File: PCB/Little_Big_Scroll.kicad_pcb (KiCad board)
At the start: 2 copper layers, 83.6 x 40 mm, 22 parts, among them J1 Conn_01x02, SW1 SW_Push, SW2 SW_Push, SW3 SW_Push, SW4 SW_Push, SW7 Rotary_Encoder_Switch, U1 ProMicro

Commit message: folders
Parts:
- added Lic1: CC-BY-SA_4.0, Keyboard Library:CC_BY_SA_40, F.Cu at (234.2, 111.9)
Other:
- board text added: "JLCJLCJLCJLC"
- board text added: "Little Big Scroll v1.0 Markus Knutsson 2021 https://github.com/TweetyDaBird"
- board text removed: "Little Big Scroll v1.0 Markus Knutsson 2021 https://github.com/TweetyDaBird Licensed under CERN-OHL-S v2+ JLCJLCJLCJLC"

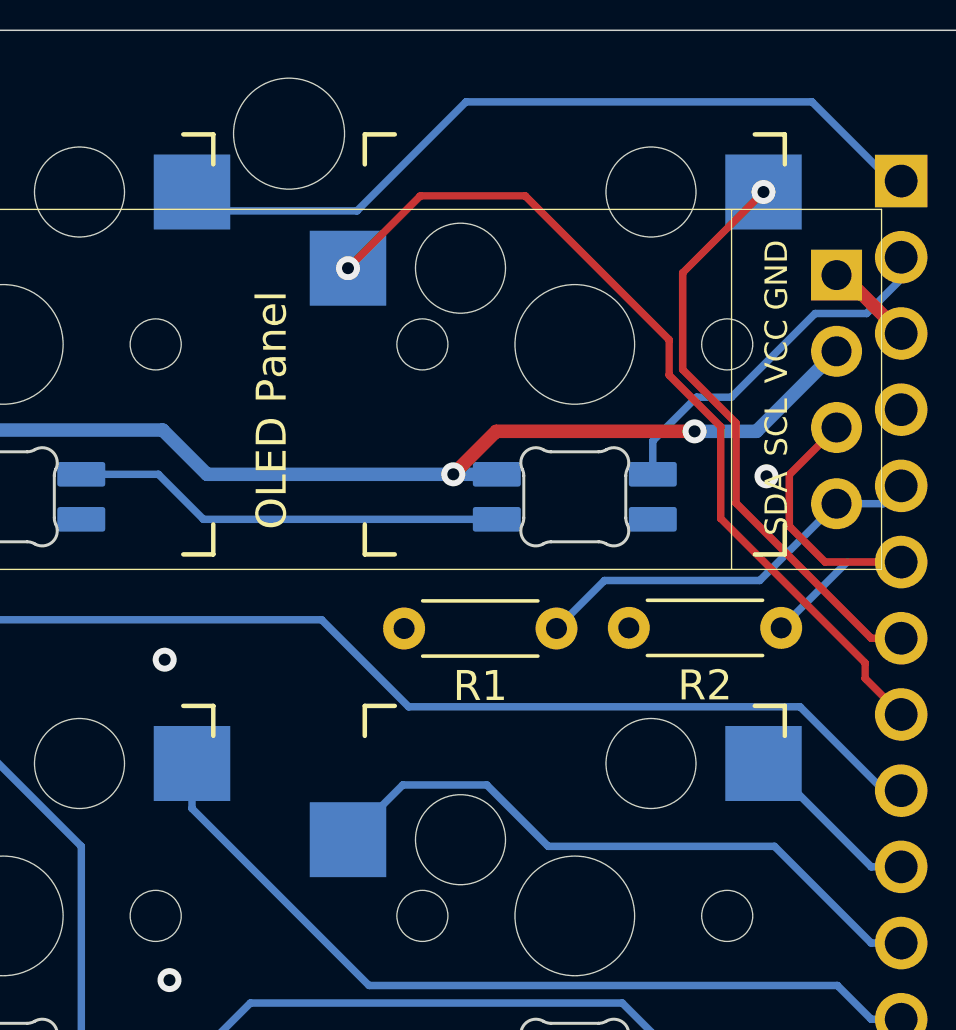
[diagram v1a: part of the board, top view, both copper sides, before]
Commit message: Added licensing on PCB
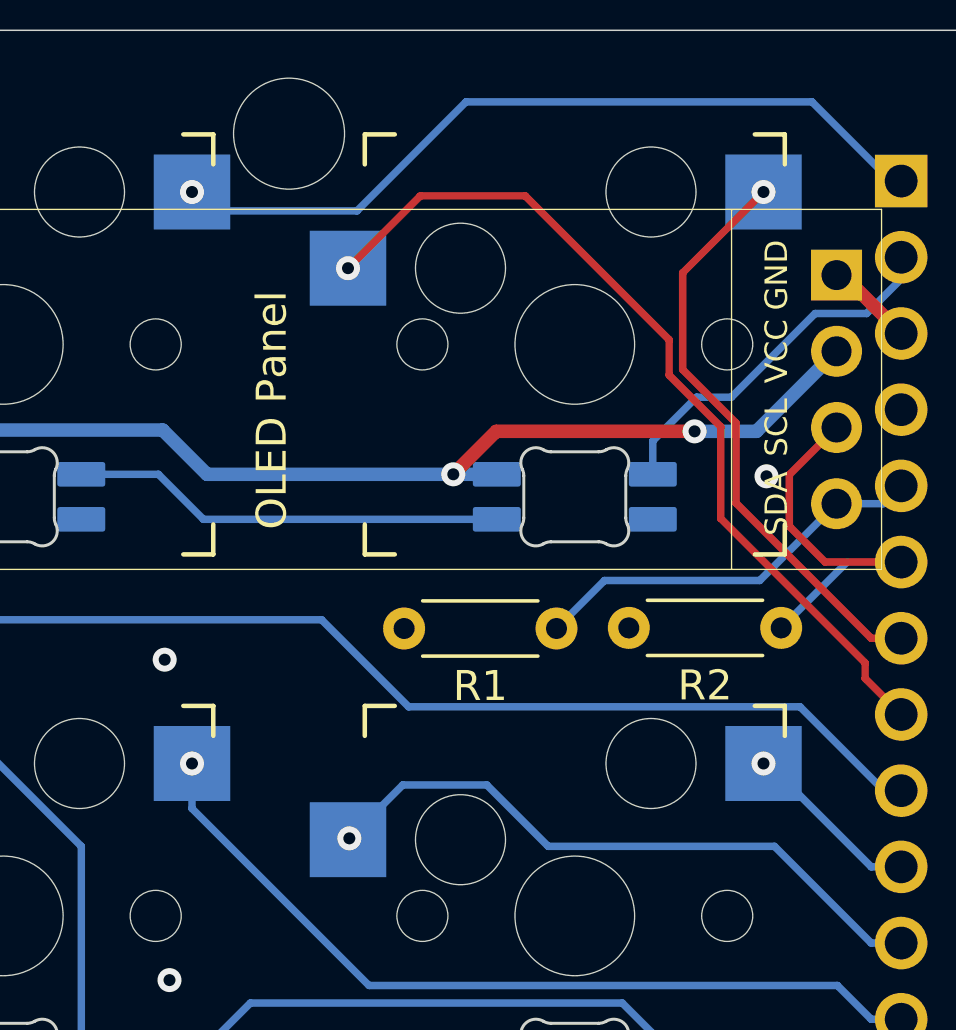
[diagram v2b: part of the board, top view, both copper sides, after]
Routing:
- net ROW3: vias 0 -> 1
- net ROW2: vias 0 -> 1
- net ROW0: vias 0 -> 1
- net COL3: vias 0 -> 1
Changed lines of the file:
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@@
     (thickness 1.6)
     (drawings 19)
-    (tracks 187)
+    (tracks 195)
     (zones 0)
     (modules 23)
@@
     (0 F.Cu signal)
     (31 B.Cu signal)
-    (32 B.Adhes user)
-    (33 F.Adhes user)
-    (34 B.Paste user)
-    (35 F.Paste user)
+    (32 B.Adhes user hide)
+    (33 F.Adhes user hide)
+    (34 B.Paste user hide)
+    (35 F.Paste user hide)
     (36 B.SilkS user)
     (37 F.SilkS user)
-    (38 B.Mask user)
-    (39 F.Mask user)
-    (40 Dwgs.User user)
-    (41 Cmts.User user)
-    (42 Eco1.User user)
-    (43 Eco2.User user)
+    (38 B.Mask user hide)
+    (39 F.Mask user hide)
+    (40 Dwgs.User user hide)
+    (41 Cmts.User user hide)
+    (42 Eco1.User user hide)
+    (43 Eco2.User user hide)
     (44 Edge.Cuts user)
-    (45 Margin user)
-    (46 B.CrtYd user)
-    (47 F.CrtYd user)
-    (48 B.Fab user)
-    (49 F.Fab user)
+    (45 Margin user hide)
+    (46 B.CrtYd user hide)
+    (47 F.CrtYd user hide)
+    (48 B.Fab user hide)
+    (49 F.Fab user hide)
   )
   (setup
@@
     (add_net "Net-(LED4-Pad2)")
     (add_net "Net-(LED5-Pad2)")
-    (add_net "Net-(LED6-Pad2)")
-    (add_net "Net-(U1-Pad14)")
-    (add_net "Net-(U1-Pad15)")
-    (add_net "Net-(U1-Pad18)")
-    (add_net "Net-(U1-Pad24)")
     (add_net RGB)
     (add_net ROW0)
@@
     (fp_text value CC-BY-SA_4.0 (at -0.19 -3.93 90) (layer F.Fab)
       (effects (font (size 0.8 0.8) (thickness 0.15)))
-    )
-    (fp_text user "CC BY-SA 4.0" (at -0.041555 2.16 90) (layer F.SilkS)
-      (effects (font (size 0.8 0.8) (thickness 0.15)))
-    )
-    (fp_text user https://creativecommons.org (at -0.041555 3.07 90) (layer F.SilkS)
-      (effects (font (size 0.5 0.5) (thickness 0.1)))
     )
     (fp_poly (pts (xy 2.926022 -0.651376) (xy 3.024018 -0.638898) (xy 3.07798 -0.626859) (xy 3.140861 -0.606141)
@@
       (xy -3.12864 -1.278275) (xy -3.086969 -1.279086) (xy -3.035172 -1.27953) (xy -2.971261 -1.279704)
       (xy -2.956311 -1.279715) (xy -2.889956 -1.279658)) (layer F.SilkS) (width 0.01))
+    (fp_text user "CC BY-SA 4.0" (at -0.041555 2.16 90) (layer F.SilkS)
+      (effects (font (size 0.8 0.8) (thickness 0.15)))
+    )
+    (fp_text user https://creativecommons.org (at -0.041555 3.07 90) (layer F.SilkS)
+      (effects (font (size 0.5 0.5) (thickness 0.1)))
+    )
   )
   (module Keebio-Parts:RotaryEncoder_Alps_EC11E-Switch_Vertical_H20mm (layer F.Cu)
@@
   (segment (start 195.925 96.585) (end 193.284999 93.944999) (width 0.25) (layer B.Cu) (net 14) (status 10))
   (segment (start 196.26 96.585) (end 195.925 96.585) (width 0.25) (layer B.Cu) (net 14) (status 30))
+  (segment (start 172.62 96.95) (end 172.62 96.95) (width 0.25) (layer B.Cu) (net 14) (status 30))
+  (via (at 172.62 96.95) (size 0.8) (drill 0.4) (layers F.Cu B.Cu) (net 14))
   (via (at 177.82 99.49) (size 0.8) (drill 0.4) (layers F.Cu B.Cu) (net 15) (status 30))
   (segment (start 195.058699 113.163699) (end 196.26 114.365) (width 0.25) (layer F.Cu) (net 15) (status 20))
@@
   (segment (start 195.26 124.525) (end 194.133901 123.398901) (width 0.25) (layer B.Cu) (net 18))
   (segment (start 196.26 124.525) (end 195.26 124.525) (width 0.25) (layer B.Cu) (net 18) (status 10))
-  (segment (start 179.645001 116.714999) (end 177.82 118.54) (width 0.25) (layer B.Cu) (net 19) (status 20))
+  (segment (start 172.62 116) (end 172.62 116) (width 0.25) (layer B.Cu) (net 18) (status 20))
+  (via (at 172.62 116) (size 0.8) (drill 0.4) (layers F.Cu B.Cu) (net 18))
+  (segment (start 179.645001 116.714999) (end 177.865 118.495) (width 0.25) (layer B.Cu) (net 19) (status 20))
   (segment (start 182.446001 116.714999) (end 179.645001 116.714999) (width 0.25) (layer B.Cu) (net 19))
   (segment (start 184.492101 118.761099) (end 182.446001 116.714999) (width 0.25) (layer B.Cu) (net 19))
@@
   (segment (start 195.26 121.985) (end 192.036099 118.761099) (width 0.25) (layer B.Cu) (net 19))
   (segment (start 196.26 121.985) (end 195.26 121.985) (width 0.25) (layer B.Cu) (net 19) (status 10))
+  (segment (start 177.865 118.495) (end 177.82 118.54) (width 0.25) (layer B.Cu) (net 19) (status 20))
+  (via (at 177.865 118.495) (size 0.8) (drill 0.4) (layers F.Cu B.Cu) (net 19))
   (segment (start 195.26 119.445) (end 191.815 116) (width 0.25) (layer B.Cu) (net 20) (status 20))
   (segment (start 191.815 116) (end 191.67 116) (width 0.25) (layer B.Cu) (net 20) (status 30))
   (segment (start 196.26 119.445) (end 195.26 119.445) (width 0.25) (layer B.Cu) (net 20) (status 10))
+  (segment (start 191.67 116) (end 191.67 116) (width 0.25) (layer B.Cu) (net 20) (status 30))
+  (via (at 191.67 116) (size 0.8) (drill 0.4) (layers F.Cu B.Cu) (net 20))
   (segment (start 212.5 106.745) (end 211.5 106.745) (width 0.25) (layer F.Cu) (net 21) (status 20))
   (segment (start 214.69 104.555) (end 212.5 106.745) (width 0.25) (layer F.Cu) (net 21))

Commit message: Tweaked for v1.1
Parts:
- R1, R2: footprint Resistor_THT:R_Axial_DIN0204_L3.6mm_D1.6mm_P5.08mm_Horizontal -> Resistor_THT:R_Axial_DIN0207_L6.3mm_D2.5mm_P7.62mm_Horizontal
- SW5: renamed from SW7; footprint Keebio-Parts:RotaryEncoder_Alps_EC11E-Switch_Vertical_H20mm -> Keyboard Library:RotaryEncoder_Alps_EC11E-Switch_Vertical_H20mm
- moved R1 2.66 mm to (182.1, 111.5)
- moved C2 0.50 mm to (224.0, 126.7)
- moved J1 0.36 mm to (214.9, 93.5)
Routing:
- net SDA: track 13.5 -> 16.1 mm
- net GND: track 2.96 -> 5.50 mm, vias 9 -> 10
- net COL0: track 48.4 -> 47.2 mm
- net ROW2: track 28.0 -> 29.0 mm
- net VCC: track 186.8 -> 186.2 mm
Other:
- outline, holes or cut-outs redrawn
- board text added: "Little Big Scroll v1.1 Markus Knutsson 2022 https://github.com/TweetyDaBird"
- board text removed: "Little Big Scroll v1.0 Markus Knutsson 2021 https://github.com/TweetyDaBird"
